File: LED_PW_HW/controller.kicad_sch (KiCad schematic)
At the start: 0 parts

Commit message: imported first footprints to pcb to get an idea
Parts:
- added BT1: Battery_Holder, LED_PW_HW_Library:SMTU2032-LF, symbol LED_PW_HW_Library:Battery_Holder
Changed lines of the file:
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@@
 (kicad_sch (version 20211123) (generator eeschema)
   (paper "A4")
+  (symbol (lib_id "LED_PW_HW_Library:Battery_Holder") (at 62.23 100.33 0) (unit 1)
+    (in_bom yes) (on_board yes) (fields_autoplaced)
+    (property "Reference" "BT1" (id 0) (at 66.04 97.0279 0)
+      (effects (font (size 1.27 1.27)) (justify left))
+    )
+    (property "Value" "Battery_Holder" (id 1) (at 66.04 99.5679 0)
+      (effects (font (size 1.27 1.27)) (justify left))
+    )
+    (property "Footprint" "LED_PW_HW_Library:SMTU2032-LF" (id 2) (at 62.23 98.806 90)
+      (effects (font (size 1.27 1.27)) hide)
+    )
+    (property "Datasheet" "~" (id 3) (at 62.23 98.806 90)
+      (effects (font (size 1.27 1.27)) hide)
+    )
+    (pin "1")
+    (pin "2")
+  )
 )

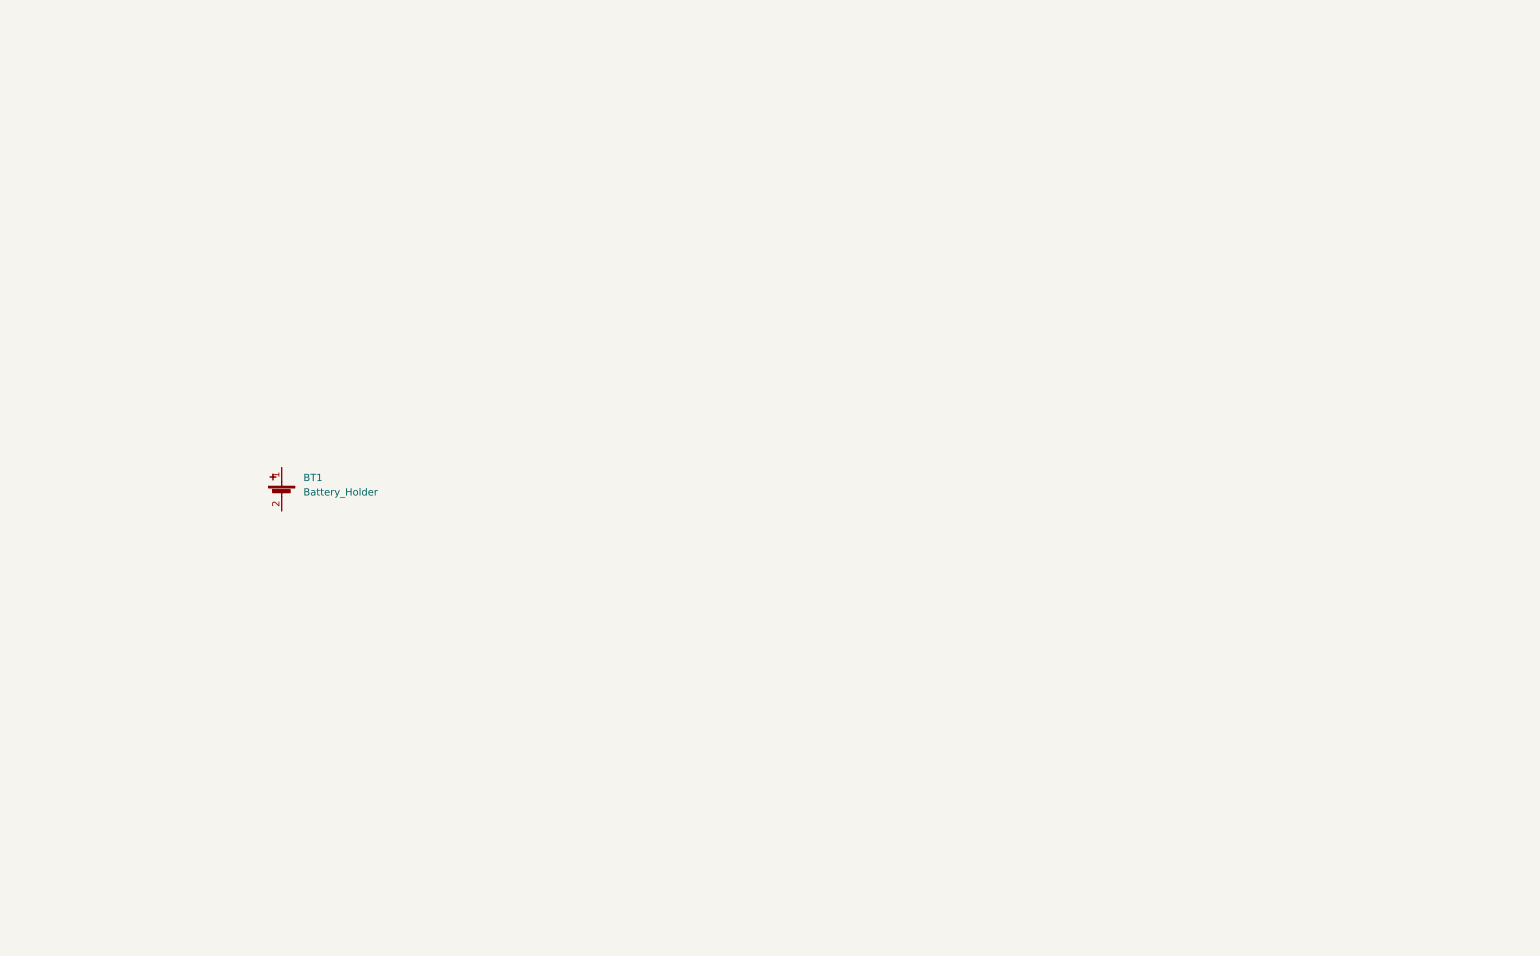
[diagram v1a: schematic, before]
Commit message: schematic of led driver part done
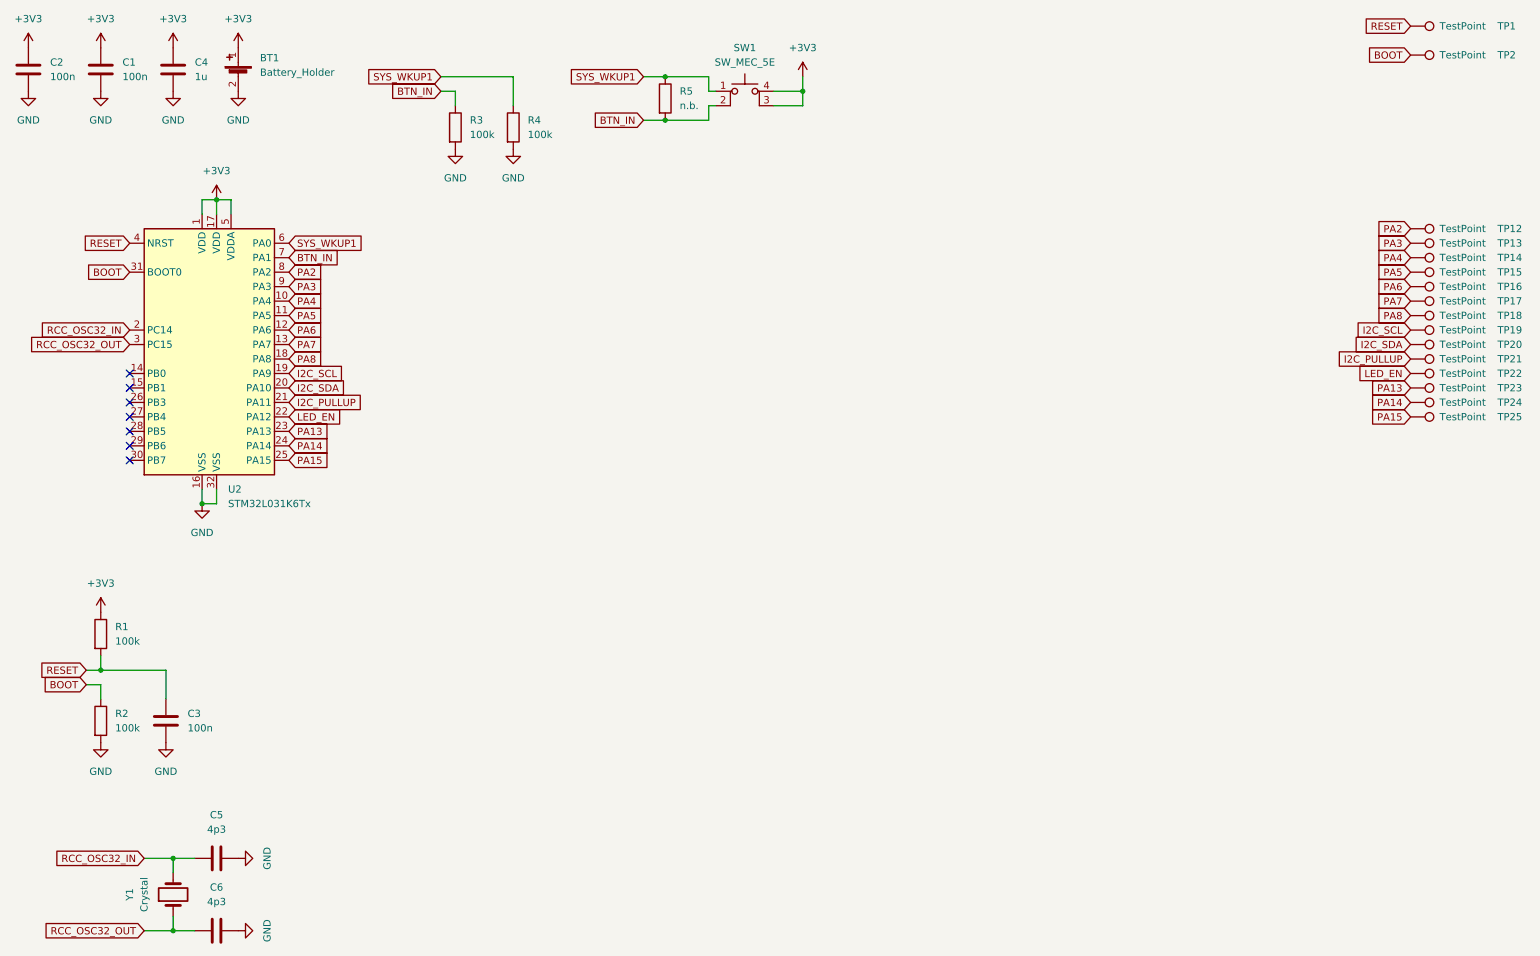
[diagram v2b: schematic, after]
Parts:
- added C1, C2, C3: 100n, Capacitor_SMD:C_0603_1608Metric_Pad1.08x0.95mm_HandSolder, symbol Device:C
- added C4: 1u, Capacitor_SMD:C_0603_1608Metric_Pad1.08x0.95mm_HandSolder, symbol Device:C
- added C5, C6: 4p3, Capacitor_SMD:C_0402_1005Metric_Pad0.74x0.62mm_HandSolder, symbol Device:C
- added R1, R2, R3, R4: 100k, Resistor_SMD:R_0603_1608Metric_Pad0.98x0.95mm_HandSolder, symbol Device:R
- added R5: n.b., Resistor_SMD:R_0603_1608Metric_Pad0.98x0.95mm_HandSolder, symbol Device:R
- added SW1: SW_MEC_5E, symbol Switch:SW_MEC_5E
- added TP1, TP12, TP13, TP14, TP15, TP16, TP17, TP18, TP19, TP2, TP20, TP21, TP22, TP23, TP24, TP25: TestPoint, TestPoint:TestPoint_Pad_D1.5mm, symbol Connector:TestPoint
- added U2: STM32L031K6Tx, Package_QFP:LQFP-32_7x7mm_P0.8mm, symbol MCU_ST_STM32L0:STM32L031K6Tx
- added Y1: Crystal, symbol Device:Crystal
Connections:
- net +3V3: now reaches BT1.1 (+)
- net +3V3: now also C1.1, C2.1, C4.1, R1.1, SW1.3 (K), SW1.4 (A), U2.1 (VDD), U2.17 (VDD), U2.5 (VDDA)
- net GND: now reaches BT1.2 (-)
- net GND: now also C1.2, C2.2, C3.2, C4.2, C5.2, C6.2, R2.2, R3.2, R4.2, U2.16 (VSS), U2.32 (VSS)
- new net BOOT: R2.1, TP2.1, U2.31 (BOOT0)
- new net BTN_IN: R3.1, R5.2, SW1.2, U2.7 (PA1)
- new net I2C_PULLUP: TP21.1, U2.21 (PA11)
- new net I2C_SCL: TP19.1, U2.19 (PA9)
- new net I2C_SDA: TP20.1, U2.20 (PA10)
- new net LED_EN: TP22.1, U2.22 (PA12)
- new net PA13: TP23.1, U2.23 (PA13)
- new net PA14: TP24.1, U2.24 (PA14)
- new net PA15: TP25.1, U2.25 (PA15)
- new net PA2: TP12.1, U2.8 (PA2)
- new net PA3: TP13.1, U2.9 (PA3)
- new net PA4: TP14.1, U2.10 (PA4)
- new net PA5: TP15.1, U2.11 (PA5)
- new net PA6: TP16.1, U2.12 (PA6)
- new net PA7: TP17.1, U2.13 (PA7)
- new net PA8: TP18.1, U2.18 (PA8)
- new net RCC_OSC32_IN: C5.1, U2.2 (PC14), Y1.2
- new net RCC_OSC32_OUT: C6.1, U2.3 (PC15), Y1.1
- new net RESET: C3.1, R1.2, TP1.1, U2.4 (NRST)
- new net SYS_WKUP1: R4.1, R5.1, SW1.1, U2.6 (PA0)
- no-connect marks 0 -> 7
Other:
- moved on the sheet: BT1

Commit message: controller schematic part done
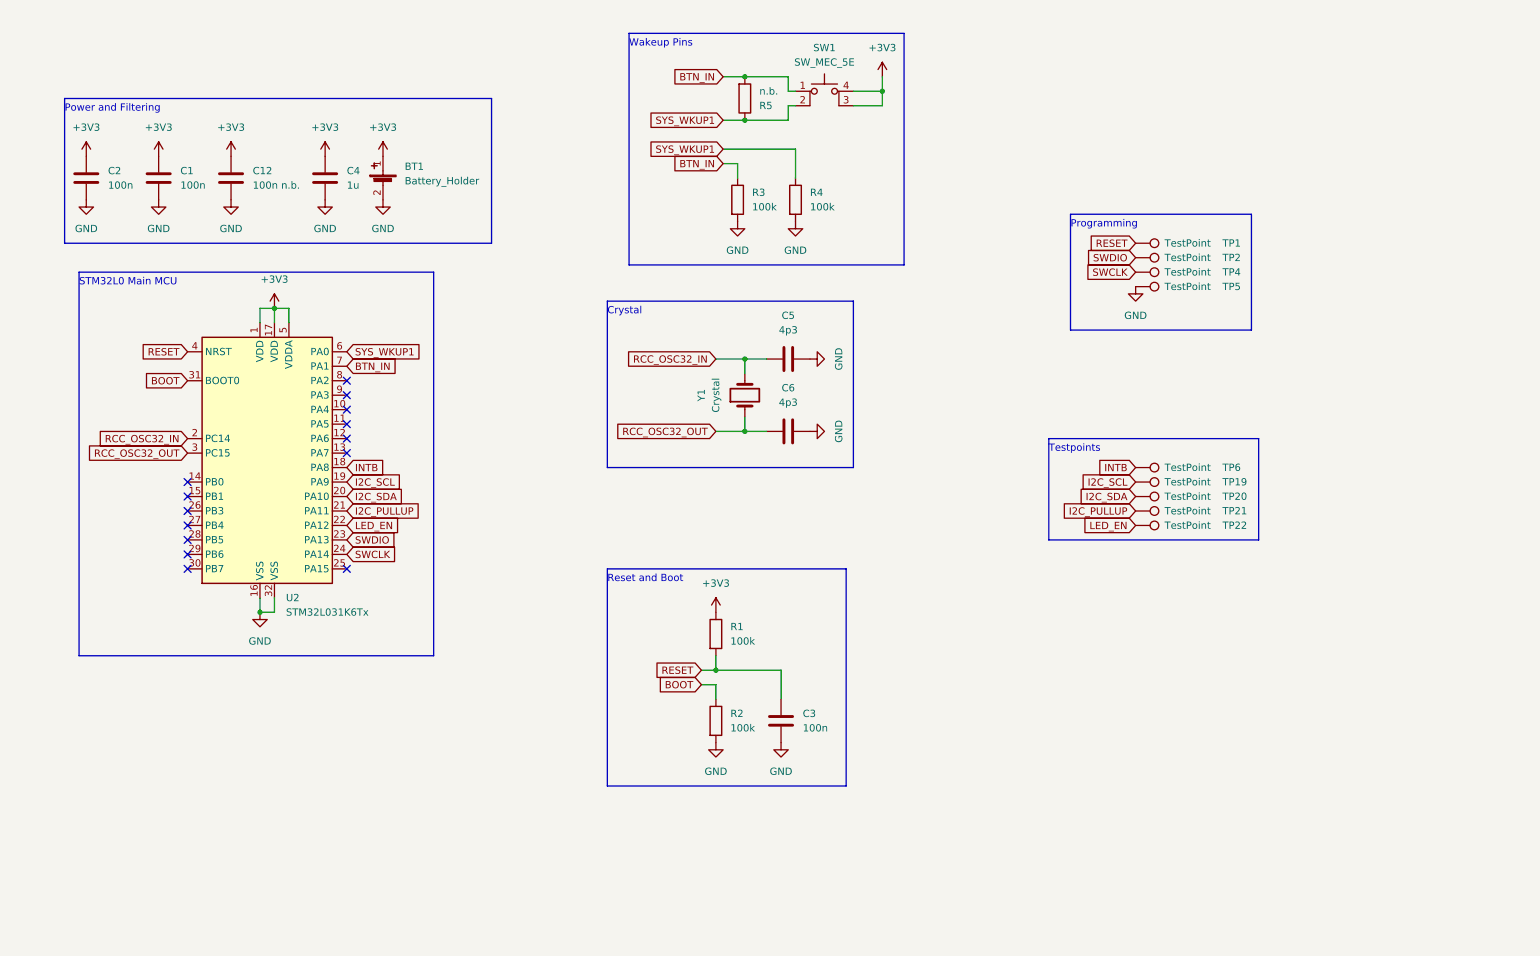
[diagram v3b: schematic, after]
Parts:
- removed TP12, TP13, TP14, TP15, TP16, TP17, TP18, TP23, TP24, TP25: TestPoint, TestPoint:TestPoint_Pad_D1.5mm, symbol Connector:TestPoint
- added C12: 100n n.b., Capacitor_SMD:C_0603_1608Metric_Pad1.08x0.95mm_HandSolder, symbol Device:C
- added TP4, TP5, TP6: TestPoint, TestPoint:TestPoint_Pad_D1.5mm, symbol Connector:TestPoint
- SW1: footprint (none) -> LED_PW_HW_Library:Switch-DifferentPadNr
- Y1: footprint (none) -> LED_PW_HW_Library:ECX-34Q
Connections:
- net +3V3: now also C12.1
- net BOOT: no longer TP2.1
- net BTN_IN: now also SW1.1; no longer SW1.2
- net GND: now also C12.2, TP5.1
- net SYS_WKUP1: now also SW1.2; no longer SW1.1
- net PA13 renamed SWDIO
- net SWDIO: now also TP2.1
- net PA14 renamed SWCLK
- net SWCLK: now also TP4.1
- net PA15: no longer names the net of U2.25 (PA15)
- net PA2: no longer names the net of U2.8 (PA2)
- net PA3: no longer names the net of U2.9 (PA3)
- net PA4: no longer names the net of U2.10 (PA4)
- net PA5: no longer names the net of U2.11 (PA5)
- net PA6: no longer names the net of U2.12 (PA6)
- net PA7: no longer names the net of U2.13 (PA7)
- net PA8 renamed INTB
- net INTB: now also TP6.1
- no-connect marks 7 -> 14
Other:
- note added: "Crystal"
- note added: "Power and Filtering"
- note added: "Programming"
- note added: "Reset and Boot"
- note added: "STM32L0 Main MCU"
- note added: "Testpoints"
- note added: "Wakeup Pins"
- moved on the sheet: BT1, C1, C2, C3, C4, C5, C6, R1, R2, R3, R4, R5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
